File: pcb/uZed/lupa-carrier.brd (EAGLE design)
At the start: 76.5 x 57.1 mm, 47 parts, among them K1 694108105102

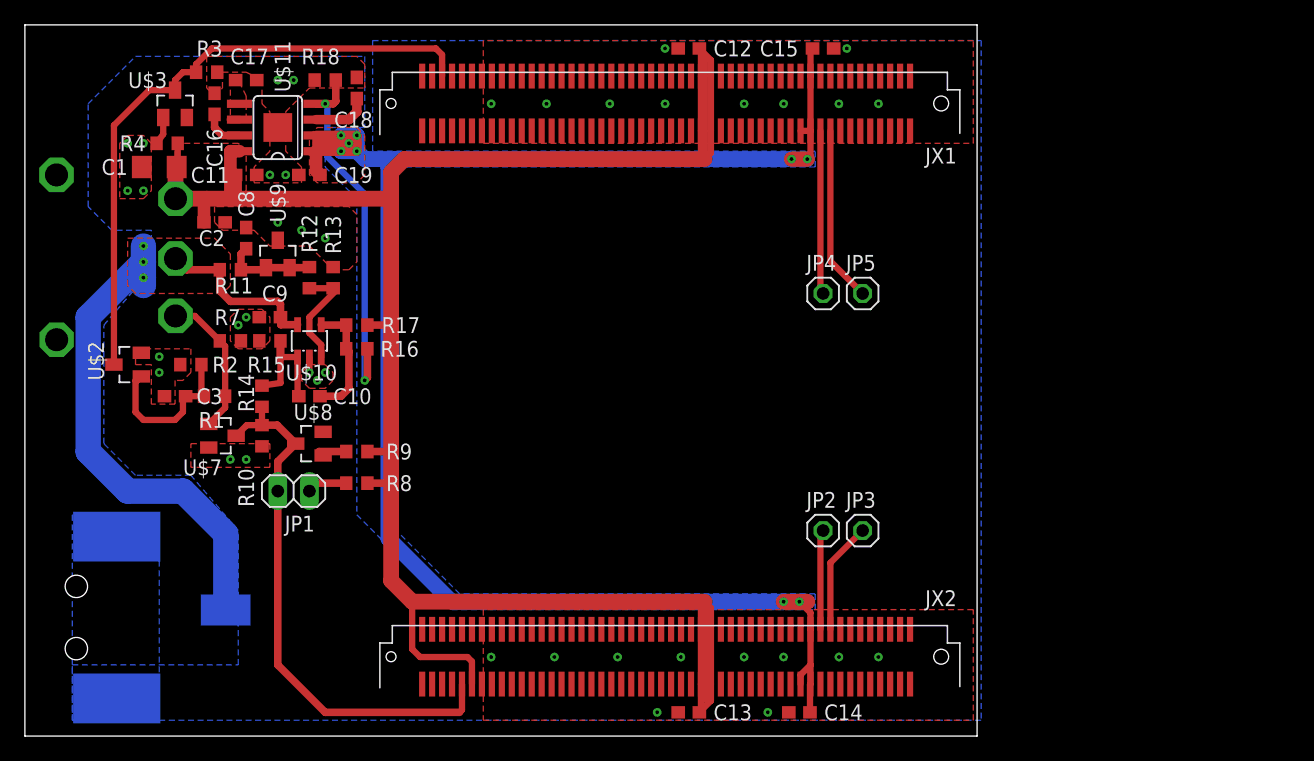
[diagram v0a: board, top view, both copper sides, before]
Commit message: started lupa300 integration, converted to 4 layer
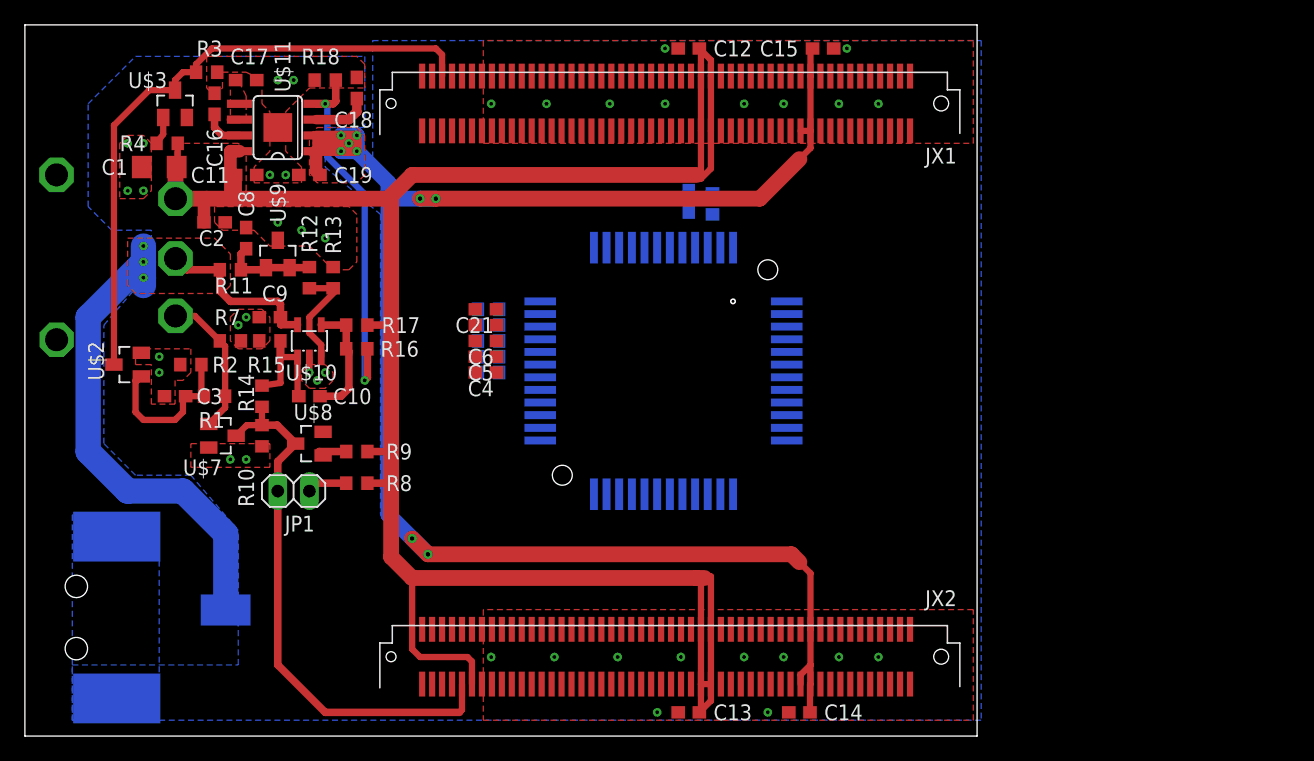
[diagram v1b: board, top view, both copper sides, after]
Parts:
- removed JP2, JP3, JP4, JP5: (no value), pinhead:1X01
- added C20, C21, C4, C6, C7: 0.1uF, rcl:C0603
- added C5: .1uF, rcl:C0603
- added R19: 110k, rcl:R0603
- added R20: 42k, rcl:R0603
- added R21: 1.5M, rcl:R0603
- added R22: 500k, rcl:R0603
- added R5: 68k, rcl:R0603
- added R6: 10k, rcl:R0603
- added U$4: (no value), andon:LUPA300
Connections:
- removed net N$13: JP2.1, JX2.P$20
- removed net N$14: JP3.1, JX2.P$18
- removed net N$15: JP4.1, JX1.P$19
- removed net N$16: JP5.1, JX1.P$17
- new net ADC_BIAS: C4.1, R6.2, U$4.P$18
- new net BIAS1: C21.1, R22.2, U$4.P$14
- new net BIAS2: C20.1, R21.2, U$4.P$15
- new net BIAS3: C6.1, R20.2, U$4.P$16
- new net BIAS4: C5.1, R19.2, U$4.P$17
- new net CLK: U$4.P$5
- new net D0: U$4.P$25
- new net D1: U$4.P$26
- new net D2: U$4.P$27
- new net D3: U$4.P$28
- new net D4: U$4.P$29
- new net D5: U$4.P$32
- new net D6: U$4.P$33
- new net D7: U$4.P$34
- new net D8: U$4.P$35
- new net D9: U$4.P$36
- new net FRAME_VALID: U$4.P$38
- new net INT_TIME1: U$4.P$11
- new net INT_TIME2: U$4.P$12
- new net INT_TIME3: U$4.P$37
- new net LINE_VALID: U$4.P$39
- new net PRECHARGE_BIAS: C7.1, R5.2, U$4.P$40
- new net RESET: U$4.P$6
- new net SPI_CLK: U$4.P$47
- new net SPI_DATA: U$4.P$46
- new net SPI_EN: U$4.P$48
- new net VADC: R6.1, U$4.P$21, U$4.P$30, U$4.P$4
- new net VDDA: R19.1, R20.1, R21.1, R22.1, U$4.P$19, U$4.P$8
- new net VDDD: U$4.P$10, U$4.P$23
- new net VDDO: U$4.P$2
- new net VMEM_H: U$4.P$45
- new net VPIX: R5.1, U$4.P$13
- new net VRESET_1: U$4.P$43
- new net VRESET_2: U$4.P$42
- new net VRESET_3: U$4.P$41
- net GND: now also C20.2, C21.2, C4.2, C5.2, C6.2, C7.2, U$4.P$1, U$4.P$20, U$4.P$22, U$4.P$24, U$4.P$3, U$4.P$31, U$4.P$44, U$4.P$7, U$4.P$9
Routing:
- net N$16: track 14.1 -> 0.00 mm
- net N$15: track 13.2 -> 0.00 mm
- net N$14: track 9.01 -> 0.00 mm
- net N$13: track 8.02 -> 0.00 mm
- net N$3: track 7.62 -> 0.00 mm
- net N$2: track 6.99 -> 0.00 mm
- net 5V: track 169.1 -> 175.2 mm
- net VCCIO: track 148.2 -> 147.4 mm

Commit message: layout out power for lupa
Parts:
- removed C20, C21, C4: 0.1uF, rcl:C0603
- removed C5: .1uF, rcl:C0603
- removed R19: 110k, rcl:R0603
- removed R20: 42k, rcl:R0603
- removed R21: 1.5M, rcl:R0603
- removed R22: 500k, rcl:R0603
- removed R5: 68k, rcl:R0603
- removed R6: 10k, rcl:R0603
- added C22, C23, C26, C27: (no value), rcl:C0603
- added C24, C25: .1uf, rcl:C0603
- added C29: 10uF, rcl:C0603
- added C30, C31: 1uF, rcl:C0603
- added R23: 68k, rcl:R0603
- added R24: 10k, rcl:R0603
- added R25: 110k, rcl:R0603
- added R26: 42k, rcl:R0603
- added R27: 1.5M, rcl:R0603
- added R28: 500k, rcl:R0603
- added U$5: ADP7158ARDZ-2.5-R7CT-ND, lupa300-components:SO08
- added U$6: XC6210B252MR-G, lupa300-components:SOT25
- C6: value 0.1uF -> 10uF
- C7: value 0.1uF -> 1uF
- moved C7 15.6 mm to (42.2, 32.1), flipped to the top
- moved U$4 10.2 mm to (68.6, 21.9)
- moved C6 5.05 mm to (38.7, 27.0)
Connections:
- net SPI_CLK renamed CPI_CLK
- net VRESET_1 renamed VRESET1
- net VRESET_2 renamed VRESET2
- net VRESET_3 renamed VRESET3
- new net GNDA: C24.1, C25.1, C26.1, C27.1, C29.2, C30.2, C31.2, C6.2, C7.2, U$4.P$20, U$4.P$3, U$4.P$7, U$5.9
- new net GNDADC: C23.1, U$4.P$22, U$4.P$31
- new net GNDD: U$4.P$24, U$4.P$9, U$6.2
- new net GNDO: U$4.P$1
- new net GND_DRIVERS: C22.1, U$4.P$44
- new net N$14: C7.1, U$5.3
- new net N$22: C30.1, U$5.7
- new net N$23: C31.1, U$5.5, U$5.6
- new net N$3: C6.1, U$5.1, U$5.2
- new net VDDA_EN: U$5.4
- new net VDDD_EN: U$6.3
- net 5V: now also C29.1, U$5.8, U$6.1
- net ADC_BIAS: now also C23.2, R24.1; no longer C4.1, R6.2
- net BIAS1: now also C27.2, R28.1; no longer C21.1, R22.2
- net BIAS2: now also C26.2, R27.1; no longer C20.1, R21.2
- net BIAS3: now also C25.2, R26.1; no longer C6.1, R20.2
- net BIAS4: now also C24.2, R25.1; no longer C5.1, R19.2
- net GND: no longer C20.2, C21.2, C4.2, C5.2, C6.2, C7.2, U$4.P$1, U$4.P$20, U$4.P$22, U$4.P$24, U$4.P$3, U$4.P$31, U$4.P$44, U$4.P$7, U$4.P$9
- net PRECHARGE_BIAS: now also C22.2, R23.1; no longer C7.1, R5.2
- net VADC: now also R24.2; no longer R6.1
- net VDDA: now also R25.2, R26.2, R27.2, R28.2; no longer R19.1, R20.1, R21.1, R22.1
- net VDDD: now also U$6.5
- net VPIX: now also R23.2; no longer R5.1
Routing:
- net BIAS2: track 0.00 -> 5.25 mm
- net BIAS1: track 0.00 -> 4.78 mm
- net BIAS3: track 0.00 -> 4.57 mm
- net BIAS4: track 0.00 -> 4.49 mm
- net ADC_BIAS: track 0.00 -> 4.46 mm, vias 0 -> 1
- net VCCIO: track 147.4 -> 146.1 mm

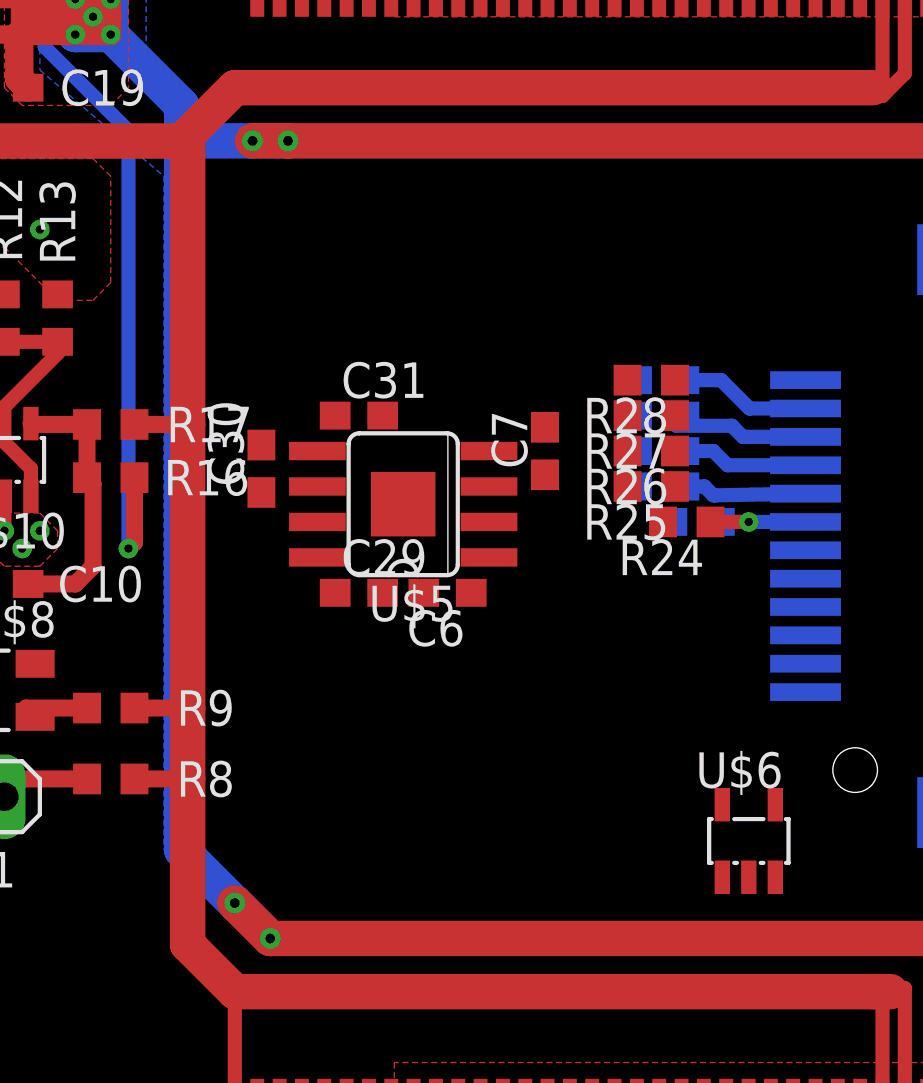
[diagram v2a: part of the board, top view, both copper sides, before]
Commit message: added low noise regulators for sensitive lupa supplys
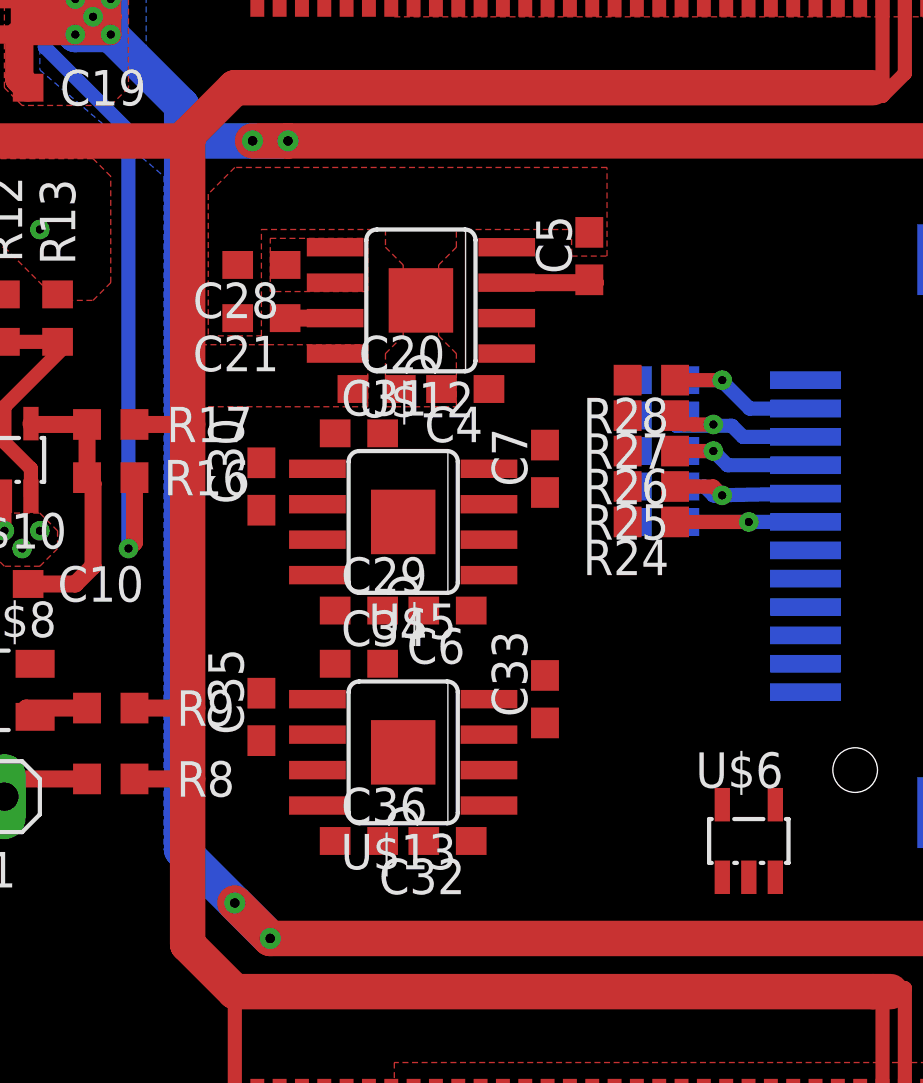
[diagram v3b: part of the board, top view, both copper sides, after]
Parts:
- added C20, C32, C36, C4: 10uF, rcl:C0603
- added C21, C28, C33, C34, C35, C5: 1uF, rcl:C0603
- added U$12, U$13: ADP7158ARDZ-2.5-R7CT-ND, lupa300-components:SO08
- moved C23 1.27 mm to (46.4, 29.5)
- moved R24 1.27 mm to (46.0, 29.5)
- moved C29 0.64 mm to (35.6, 26.4)
- moved C30 0.64 mm to (32.1, 30.8)
- moved C6 0.64 mm to (38.7, 26.4)
- moved C7 0.64 mm to (42.2, 31.4)
- moved U$5 0.64 mm to (37.1, 29.5)
- moved C31 0.63 mm to (35.6, 32.7)
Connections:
- new net N$13: C28.1, U$12.5, U$12.6
- new net N$18: C35.1, U$13.7
- new net N$19: C34.1, U$13.5, U$13.6
- new net N$2: C5.1, U$12.3
- new net N$20: C33.1, U$13.3
- new net VPIX_EN: U$12.4
- net 5V: now also C20.1, C36.1, U$12.8, U$13.8
- net GNDADC: now also C32.2, C33.2, C34.2, C35.2, C36.2, U$13.9
- net GND_DRIVERS: now also C20.2, C21.2, C28.2, C4.2, C5.2, U$12.9
- net N$3: now also C21.1, U$12.7; no longer C6.1, U$5.1, U$5.2
- net VADC: now also C32.1, U$13.1, U$13.2
- net VDDA: now also C6.1, U$5.1, U$5.2
- net VPIX: now also C4.1, U$12.1, U$12.2
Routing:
- net N$2: track 0.00 -> 3.41 mm
- net ADC_BIAS: track 4.46 -> 7.00 mm
- net BIAS4: track 4.49 -> 6.31 mm, vias 0 -> 1
- net N$3: track 0.00 -> 1.79 mm
- net BIAS1: track 4.78 -> 6.47 mm, vias 0 -> 1
- net BIAS2: track 5.25 -> 6.75 mm, vias 0 -> 1
- net BIAS3: track 4.57 -> 5.94 mm, vias 0 -> 1
- added copper zone on layer 1, net GND_DRIVERS
- added copper zone on layer 1, net N$13

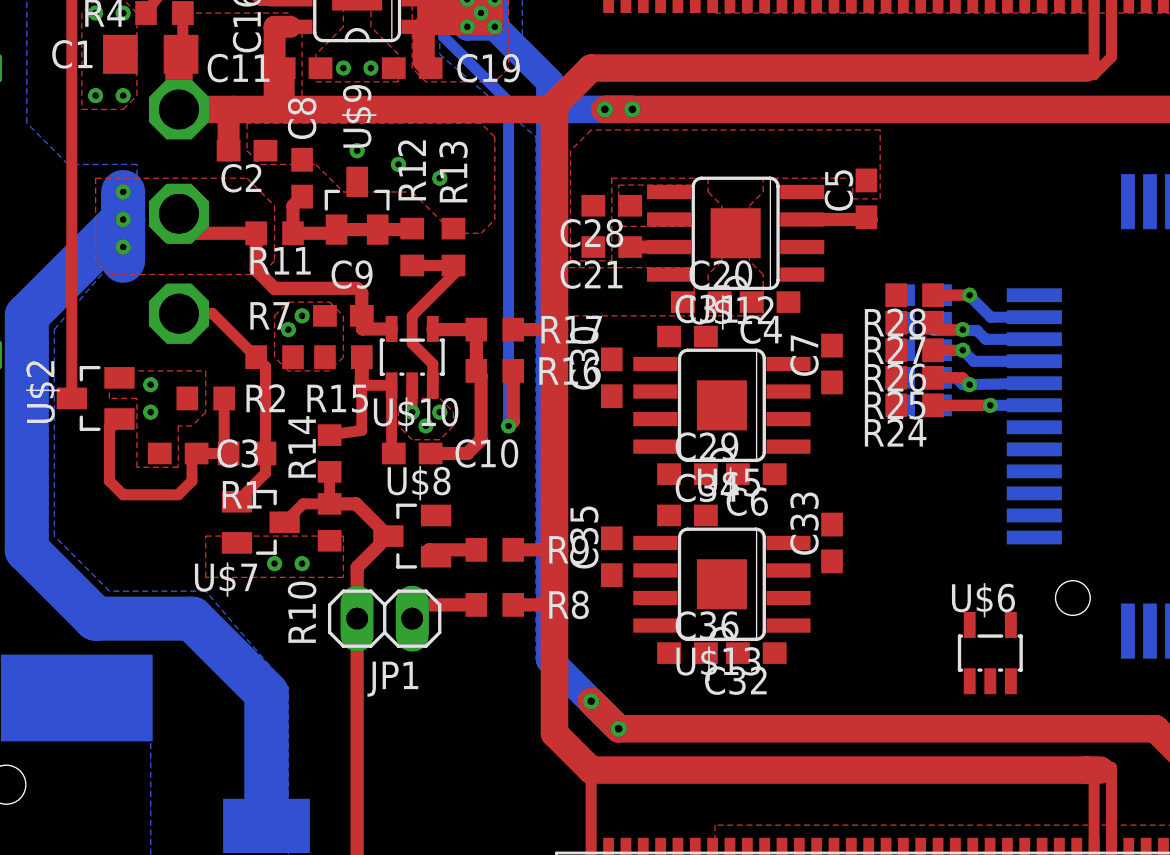
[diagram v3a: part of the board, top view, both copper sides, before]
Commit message: layed out regualtors for lupa power
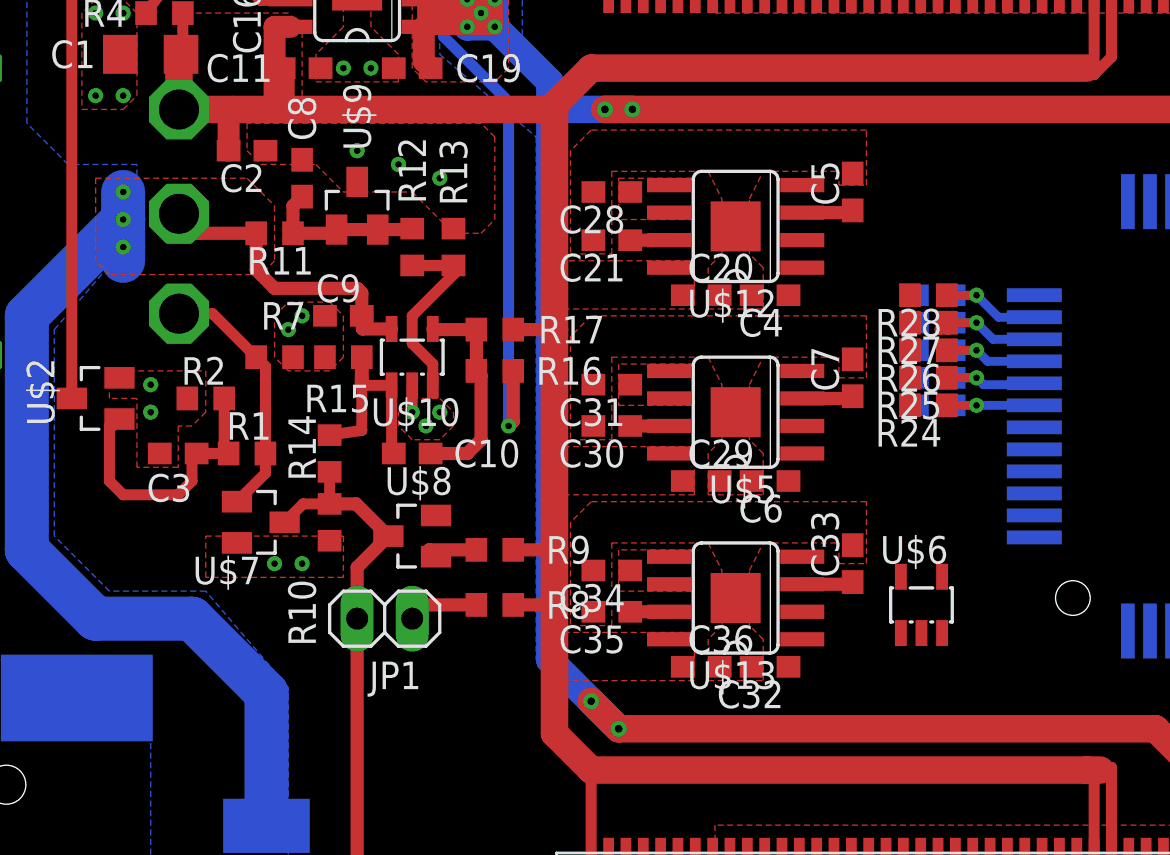
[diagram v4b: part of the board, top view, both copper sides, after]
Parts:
- moved C34 4.32 mm to (32.1, 21.9), turned to 180 degrees
- moved C31 4.14 mm to (32.1, 30.5), turned to 180 degrees
- moved U$6 3.88 mm to (46.4, 20.3)
- moved C35 2.54 mm to (32.1, 20.0), turned to 180 degrees
- moved C30 2.22 mm to (32.1, 28.6), turned to 180 degrees
- moved C33 1.35 mm to (43.2, 22.2)
- moved C7 1.14 mm to (43.2, 30.8)
- moved C32 0.90 mm to (39.4, 17.5)
- moved C36 0.90 mm to (36.2, 17.5)
- moved U$13 0.90 mm to (37.8, 20.6)
- moved C29 0.71 mm to (36.2, 26.0)
- moved C6 0.71 mm to (39.4, 26.0)
- moved U$5 0.71 mm to (37.8, 29.2)
- moved C5 0.71 mm to (43.2, 39.4)
- moved C23 0.64 mm to (47.0, 29.5)
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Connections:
- net D0: now also JX2.P$58
- net D1: now also JX2.P$60
- net D2: now also JX2.P$64
- net D3: now also JX2.P$66
- net D4: now also JX2.P$70
- net D5: now also JX2.P$72
- net D6: now also JX2.P$76
- net D7: now also JX2.P$78
- net D8: now also JX2.P$82
- net D9: now also JX2.P$84
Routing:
- net N$14: track 0.00 -> 2.37 mm
- net N$20: track 0.00 -> 2.37 mm
- net ADC_BIAS: track 7.00 -> 5.09 mm
- net N$22: track 0.00 -> 1.79 mm
- net N$18: track 0.00 -> 1.79 mm
- net BIAS4: track 6.31 -> 5.25 mm
- net BIAS1: track 6.47 -> 5.52 mm
- net BIAS2: track 6.75 -> 5.86 mm
- net N$2: track 3.41 -> 2.60 mm
- net BIAS3: track 5.94 -> 5.30 mm
- added copper zone on layer 1, net GNDA
- added copper zone on layer 1, net GNDADC
- added copper zone on layer 1, net N$19
- added copper zone on layer 1, net N$23

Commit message: more work on power supply to lupa
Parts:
- added U$14: XC6210B252MR-G, lupa300-components:SOT25
- moved U$6 32.0 mm to (75.9, 32.7)
- moved R23 9.74 mm to (64.1, 34.9), flipped to the top, turned to 270 degrees
- moved C23 9.57 mm to (56.5, 28.6), flipped to the top, turned to 90 degrees
- moved C22 9.53 mm to (62.5, 34.9), flipped to the top, turned to 90 degrees
- moved R24 8.31 mm to (54.9, 28.6), turned to 270 degrees
- moved K1 5.43 mm to (0.00, 14.9)
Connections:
- new net VDDO_EN: U$14.3
- net 5V: now also U$14.1
- net CLK: now also JX1.P$53
- net GNDO: now also U$14.2
- net VDDO: now also U$14.5
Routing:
- net VIN: track 54.1 -> 48.0 mm
- net ADC_BIAS: track 5.09 -> 0.00 mm, vias 1 -> 0
- net VDDA: track 0.00 -> 3.96 mm, vias 0 -> 3
- net VCCIO: track 146.1 -> 147.6 mm, vias 9 -> 10
- added copper zone on layer 16, net GNDA
- added copper zone on layer 1, net VADC
- added copper zone on layer 1, net VDDA
- added copper zone on layer 1, net VPIX
- added copper zone on layer 16, net VPIX
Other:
- board size 76.5 x 57.1 mm -> 101.6 x 57.1 mm

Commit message: more work on power routing
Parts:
- moved R24 2.84 mm to (57.5, 27.3)
- moved C23 2.03 mm to (54.9, 27.3)
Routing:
- net VADC: track 0.00 -> 12.2 mm, vias 0 -> 9
- net GNDADC: track 0.00 -> 8.03 mm, vias 0 -> 16
- net ADC_BIAS: track 0.00 -> 6.53 mm, vias 0 -> 1
- net VCCIO: track 147.6 -> 141.3 mm, vias 10 -> 14
- net VDDA: track 3.96 -> 8.03 mm, vias 3 -> 9
- net VIN: track 48.0 -> 44.8 mm, vias 3 -> 9
- net GND: vias 40 -> 52
- added copper zone on layer 15, net GNDADC
- added copper zone on layer 16, net VCCIO
- added copper zone on layer 15, net VDDA
- added copper zone on layer 16, net VIN
